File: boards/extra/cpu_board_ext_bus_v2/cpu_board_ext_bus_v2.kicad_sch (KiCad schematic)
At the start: 24 parts, among them J1 Exp. Conn. A, J2 Exp. Conn. B, J3 Power, J4 Exp. Conn. C

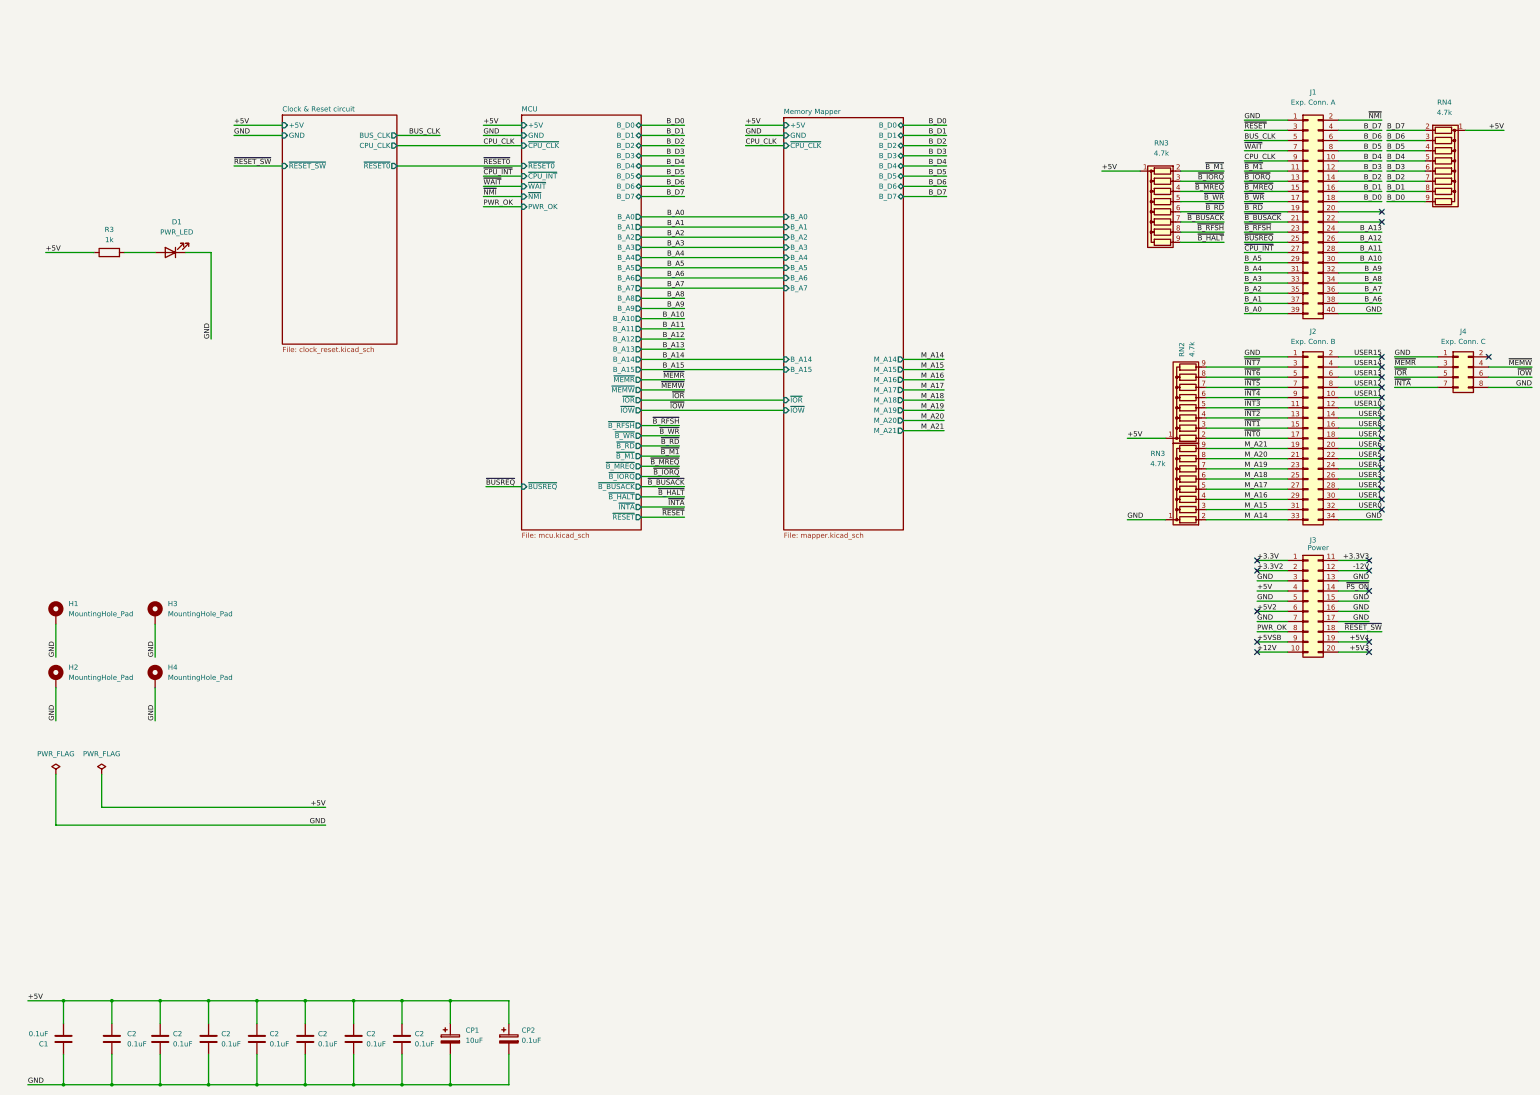
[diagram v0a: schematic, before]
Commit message: Updated CPU board V2 with extension bus
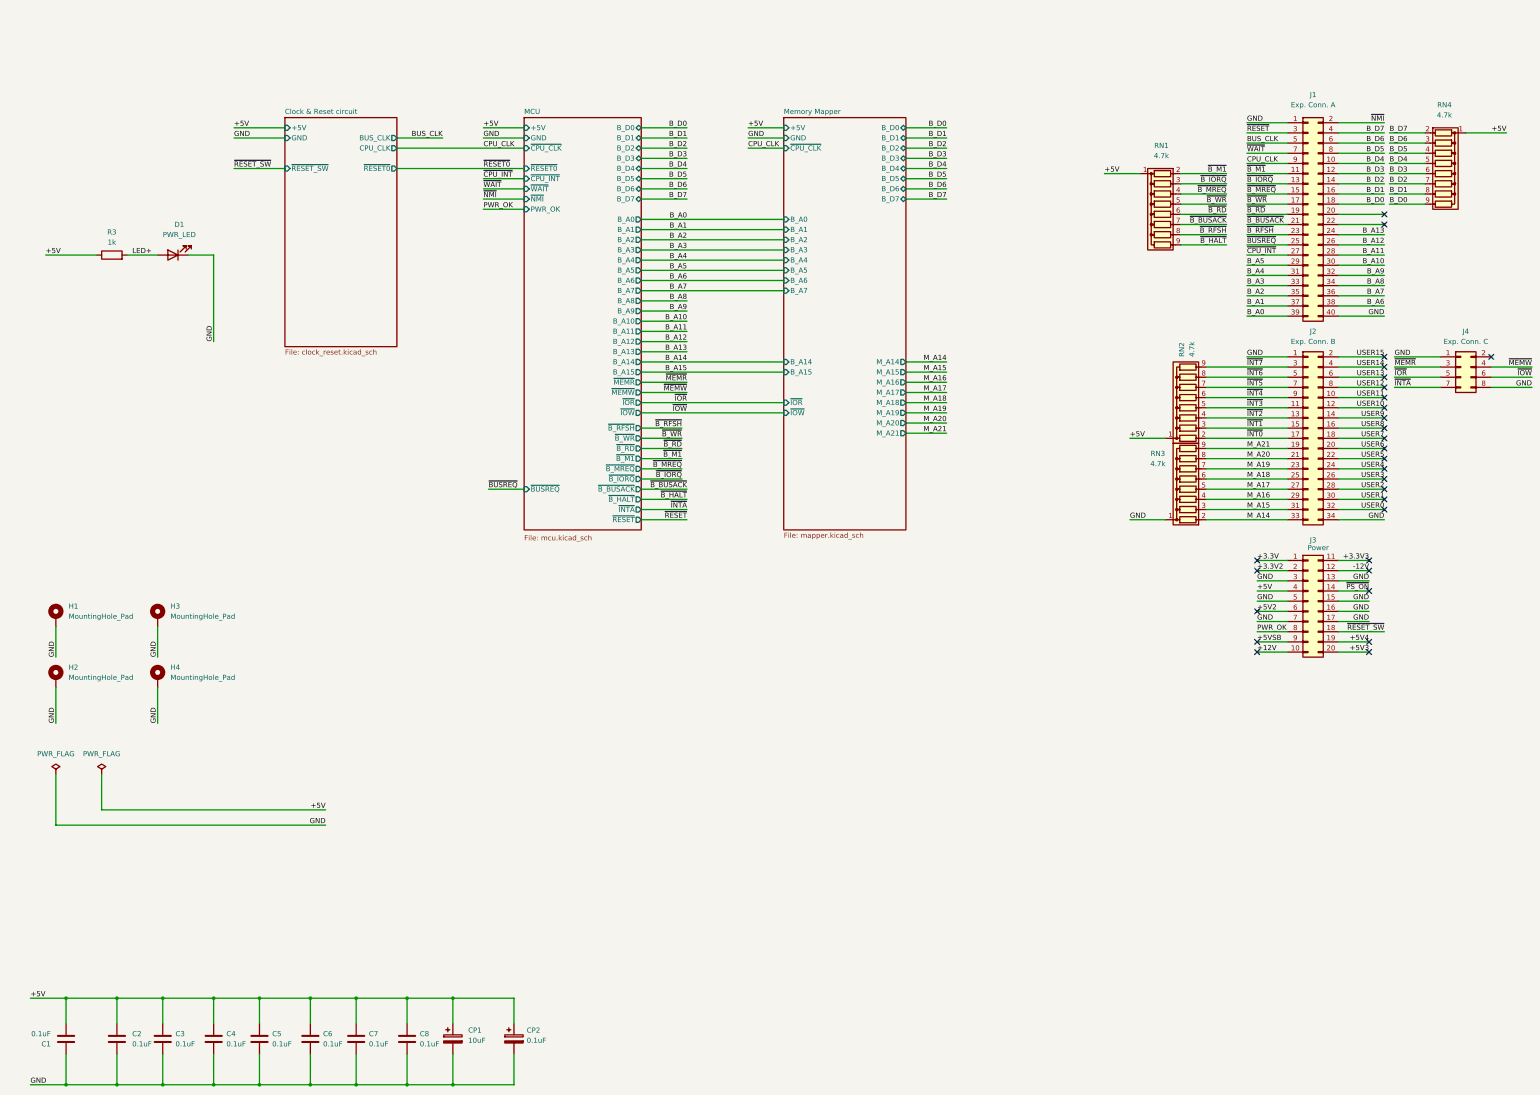
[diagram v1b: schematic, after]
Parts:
- removed C2 (x7): 0.1uF, Capacitor_THT:C_Disc_D5.0mm_W2.5mm_P2.50mm, symbol Device:C
- added C2, C3, C4, C5, C6, C7, C8: 0.1uF, Capacitor_THT:C_Disc_D5.0mm_W2.5mm_P2.50mm, symbol Device:C
- CP2: Manufacturer CX(Dongguan Chengxing Elec) -> CX(Dongguan Chengxing Elec)
- R3: MPN MFR2WSFTE73-1K -> MBA02040C1001FC100; Manufacturer YAGEO -> Vishay Intertech
- renumbered RN3 to RN1
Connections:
- net +5V: now also C2.1, C3.1, C4.1, C5.1, C6.1, C7.1, C8.1
- net GND: now also C2.2, C3.2, C4.2, C5.2, C6.2, C7.2, C8.2
- net LED+: now reaches D1.2 (A), R3.2
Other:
- moved on the sheet: D1, H1, H3, H4, J1, J4, R3, RN1, RN4

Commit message: Extended CPU board update
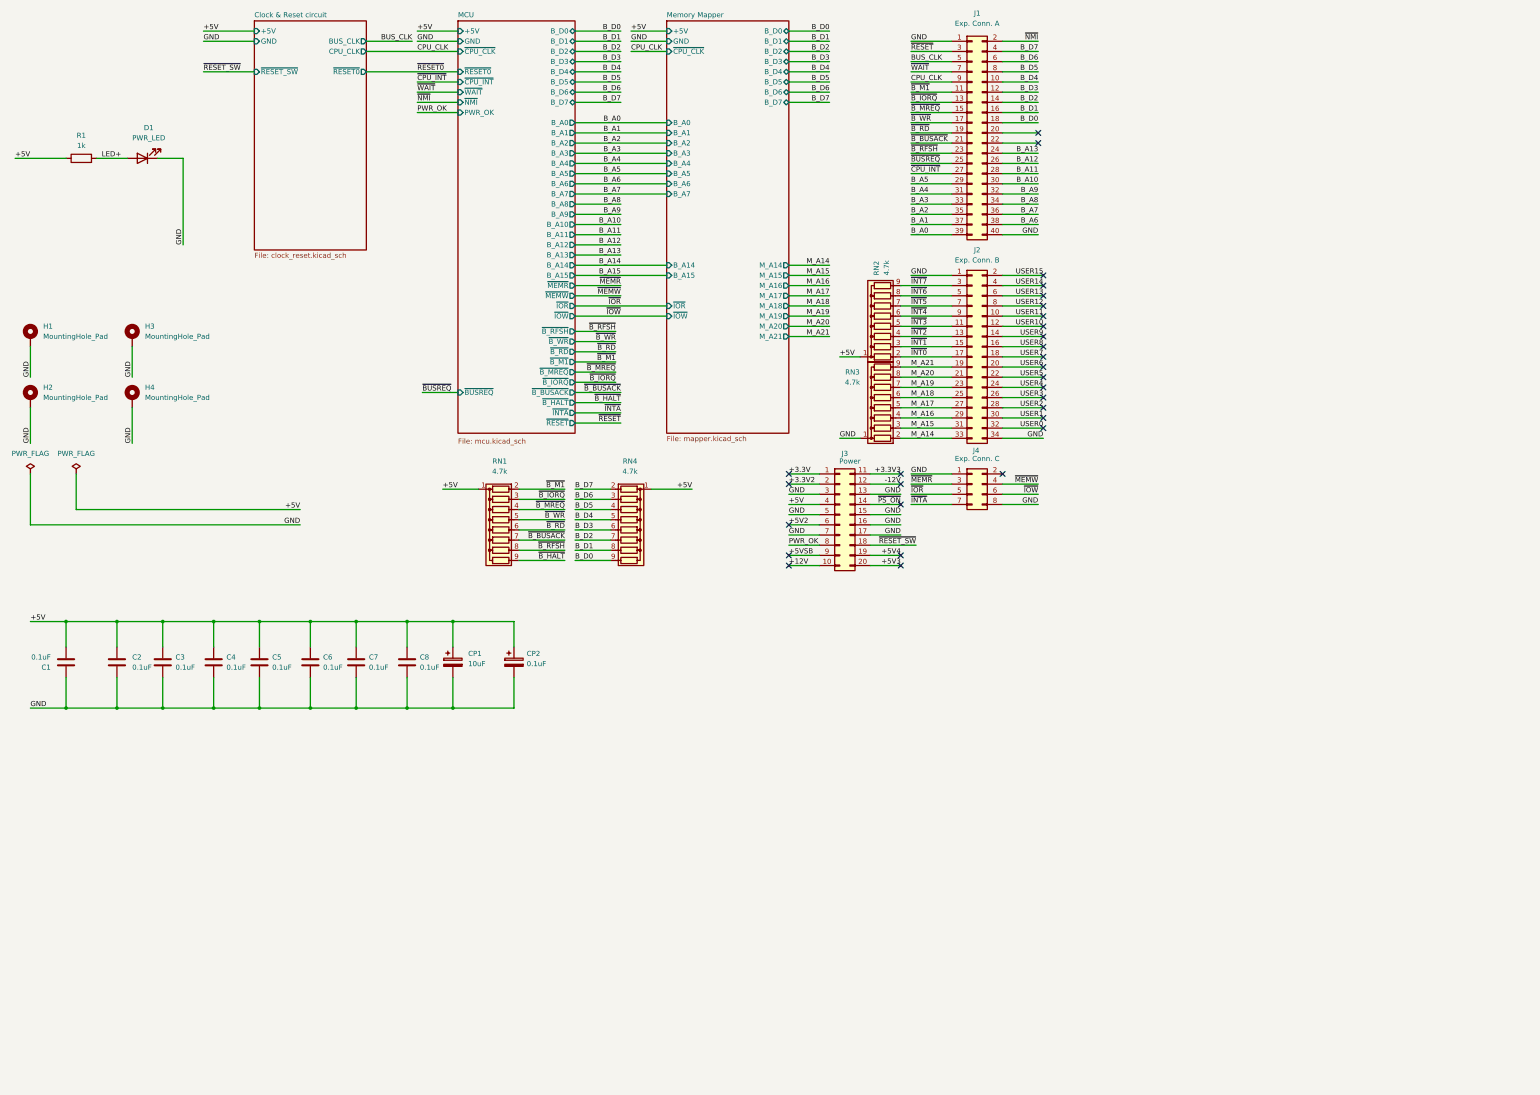
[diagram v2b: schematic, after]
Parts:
- renumbered R3 to R1
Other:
- moved on the sheet: C1, C2, C3, C4, C5, C6, C7, C8, CP1, CP2, D1, H1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
